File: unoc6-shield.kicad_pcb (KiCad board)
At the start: 2 copper layers, 78.5 x 69.7 mm, 10 parts

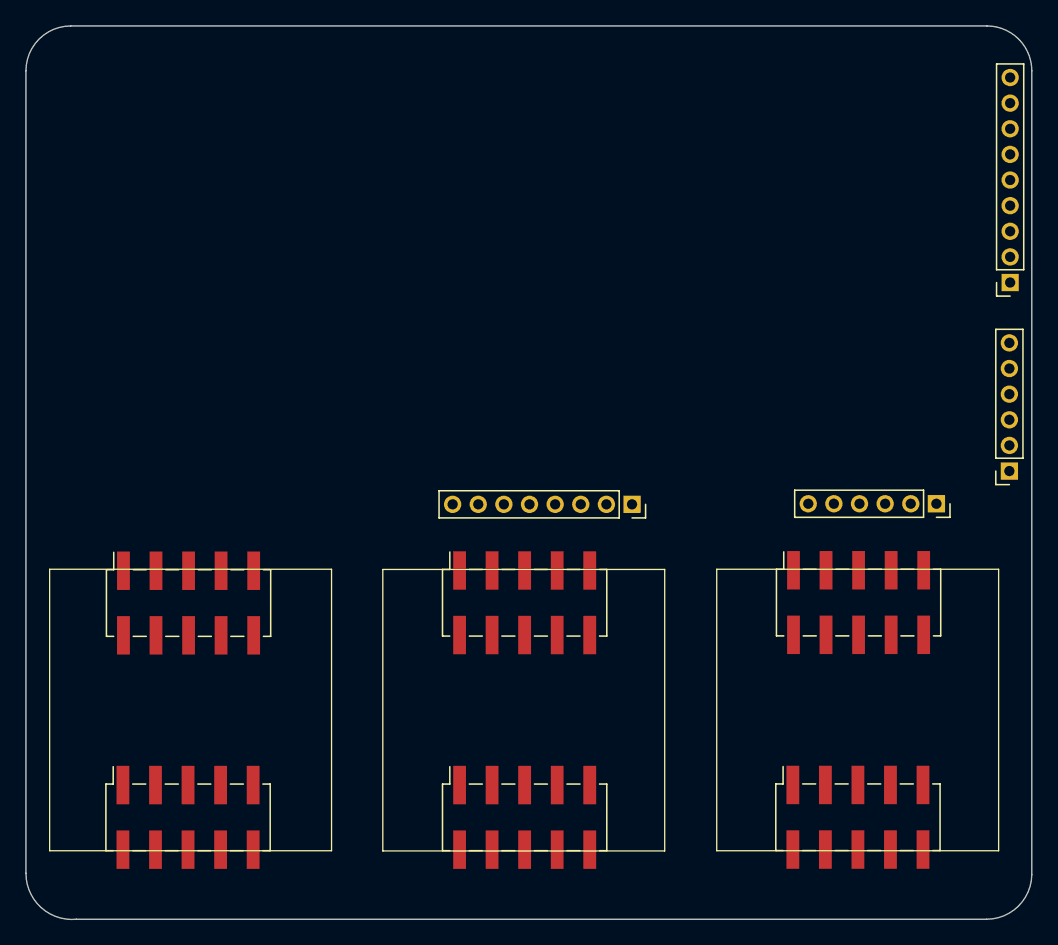
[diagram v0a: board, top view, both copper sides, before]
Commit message: ax22 pin assignment & layout restructure
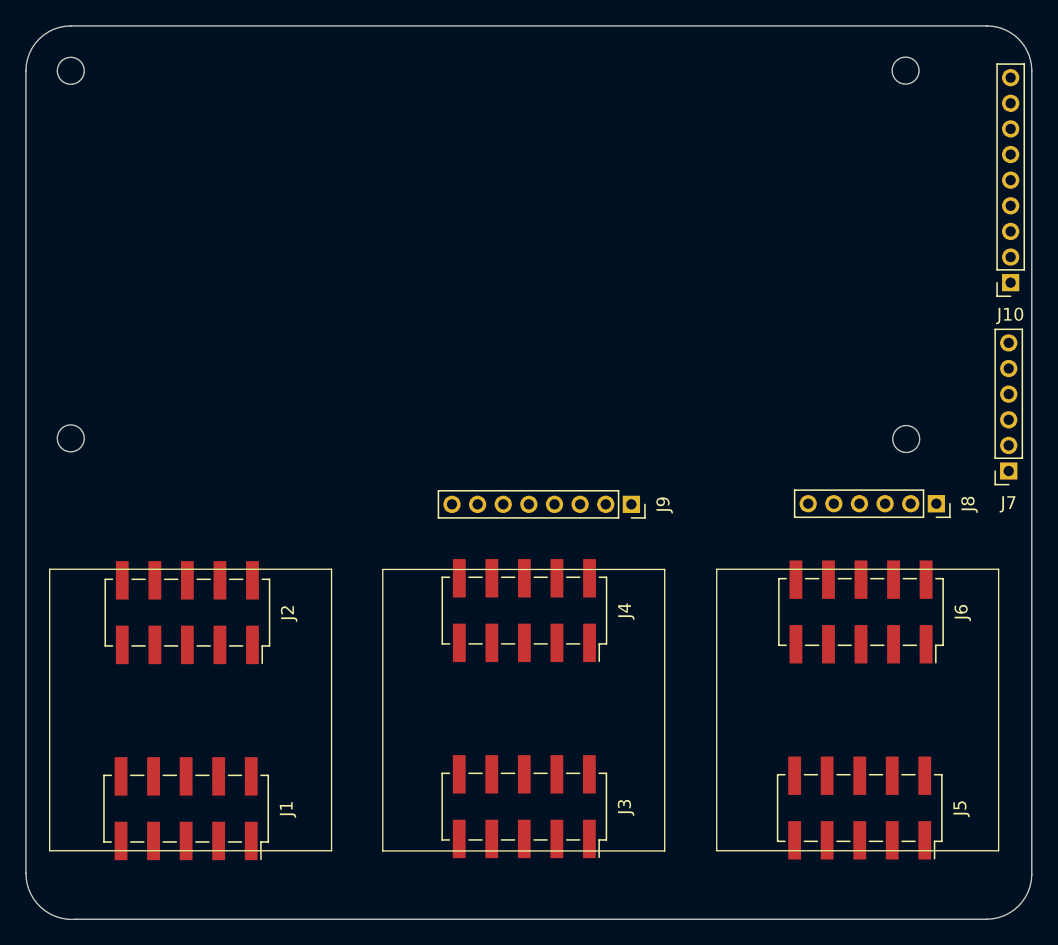
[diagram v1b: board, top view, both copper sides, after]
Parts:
- removed REF** (x6): PinSocket_2x05_P2.54mm_Vertical_SMD, Connector_PinSocket_2.54mm:PinSocket_2x05_P2.54mm_Vertical_SMD
- removed REF**: PinSocket_1x09_P2.00mm_Vertical, Connector_PinSocket_2.00mm:PinSocket_1x09_P2.00mm_Vertical
- removed REF** (x2): PinSocket_1x06_P2.00mm_Vertical, Connector_PinSocket_2.00mm:PinSocket_1x06_P2.00mm_Vertical
- removed REF**: PinSocket_1x08_P2.00mm_Vertical, Connector_PinSocket_2.00mm:PinSocket_1x08_P2.00mm_Vertical
- added H1: MountingHole, MountingHole:MountingHole_2.1mm, F.Cu at (51.8, 61.1)
- added H2: MountingHole, MountingHole:MountingHole_2.1mm, F.Cu at (51.8, 89.8)
- added H3: MountingHole, MountingHole:MountingHole_2.1mm, F.Cu at (117.0, 61.1)
- added H4: MountingHole, MountingHole:MountingHole_2.1mm, F.Cu at (117.0, 89.8)
- added J1: DIN41612_02x05_AB_EvenPins, Connector_PinSocket_2.54mm:PinSocket_2x05_P2.54mm_Vertical_SMD, F.Cu at (60.8, 118.7)
- added J10: Conn_01x09_Socket, Connector_PinSocket_2.00mm:PinSocket_1x09_P2.00mm_Vertical, F.Cu at (125.2, 77.7)
- added J2: DIN41612_02x05_AB_EvenPins, Connector_PinSocket_2.54mm:PinSocket_2x05_P2.54mm_Vertical_SMD, F.Cu at (60.9, 103.4)
- added J3: DIN41612_02x05_AB_EvenPins, Connector_PinSocket_2.54mm:PinSocket_2x05_P2.54mm_Vertical_SMD, F.Cu at (87.2, 118.5)
- added J4: DIN41612_02x05_AB_EvenPins, Connector_PinSocket_2.54mm:PinSocket_2x05_P2.54mm_Vertical_SMD, F.Cu at (87.2, 103.2)
- added J5: DIN41612_02x05_AB_EvenPins, Connector_PinSocket_2.54mm:PinSocket_2x05_P2.54mm_Vertical_SMD, F.Cu at (113.4, 118.7)
- added J6: DIN41612_02x05_AB_EvenPins, Connector_PinSocket_2.54mm:PinSocket_2x05_P2.54mm_Vertical_SMD, F.Cu at (113.5, 103.3)
- added J7: Conn_01x06_Socket, Connector_PinSocket_2.00mm:PinSocket_1x06_P2.00mm_Vertical, F.Cu at (125.0, 92.3)
- added J8: Conn_01x06_Socket, Connector_PinSocket_2.00mm:PinSocket_1x06_P2.00mm_Vertical, F.Cu at (119.3, 94.9)
- added J9: Conn_01x08_Socket, Connector_PinSocket_2.00mm:PinSocket_1x08_P2.00mm_Vertical, F.Cu at (95.5, 95.0)
